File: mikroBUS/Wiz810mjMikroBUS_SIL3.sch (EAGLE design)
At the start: 2 parts

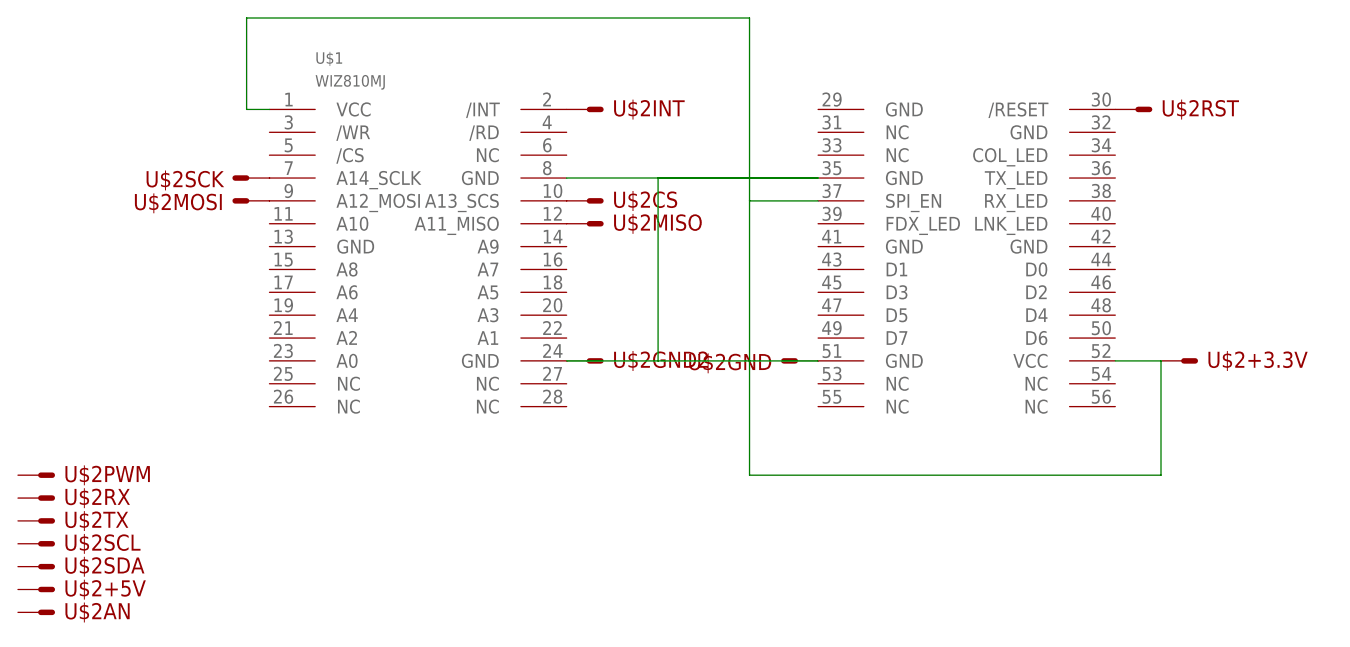
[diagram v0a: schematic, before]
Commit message: 
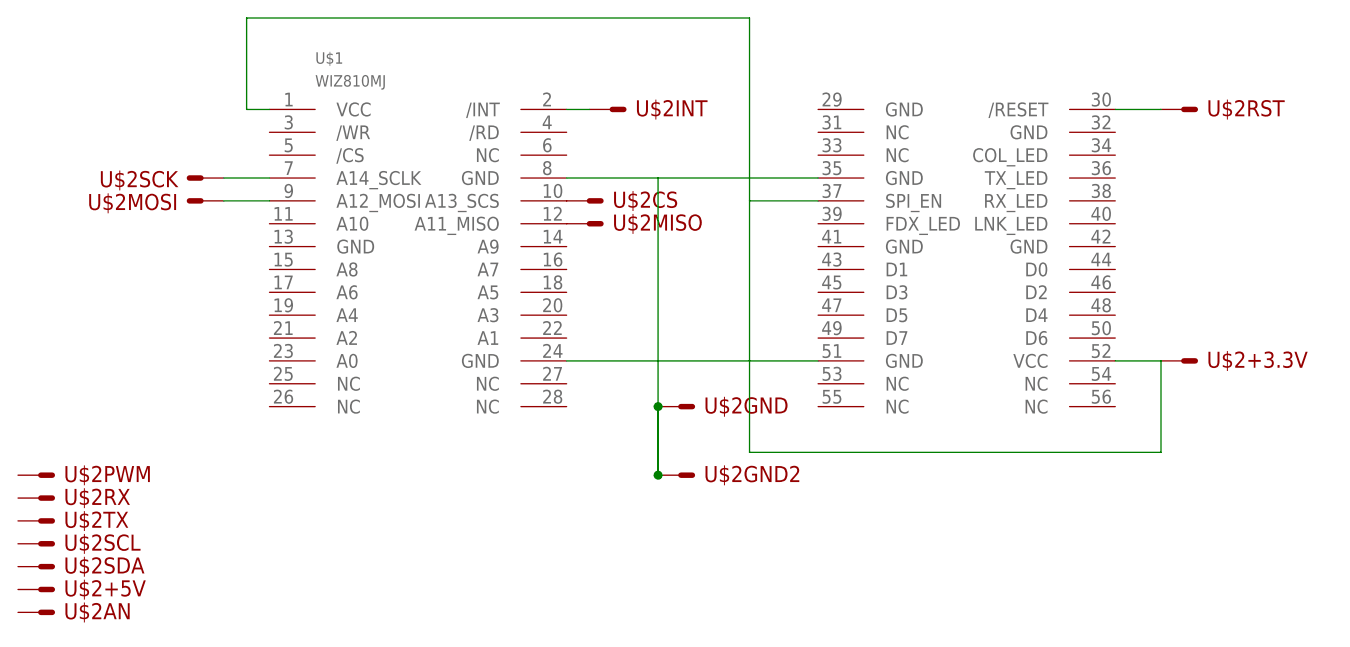
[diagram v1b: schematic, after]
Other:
- moved on the sheet: U$2GND, U$2GND2, U$2INT, U$2MOSI, U$2RST, U$2SCK
